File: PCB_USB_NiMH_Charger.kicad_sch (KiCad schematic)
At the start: 45 parts, among them J1 USB_C_Receptacle_Simple, J2 Conn_02x01, J3 Conn_02x01, J4 Conn_02x01, Q1 2SA1015, Q2 2SC1815, Q3 2SB834, Q4 2SC1815, Q5 2SB834, U1 LM393, U2 S-812C33A_TO92

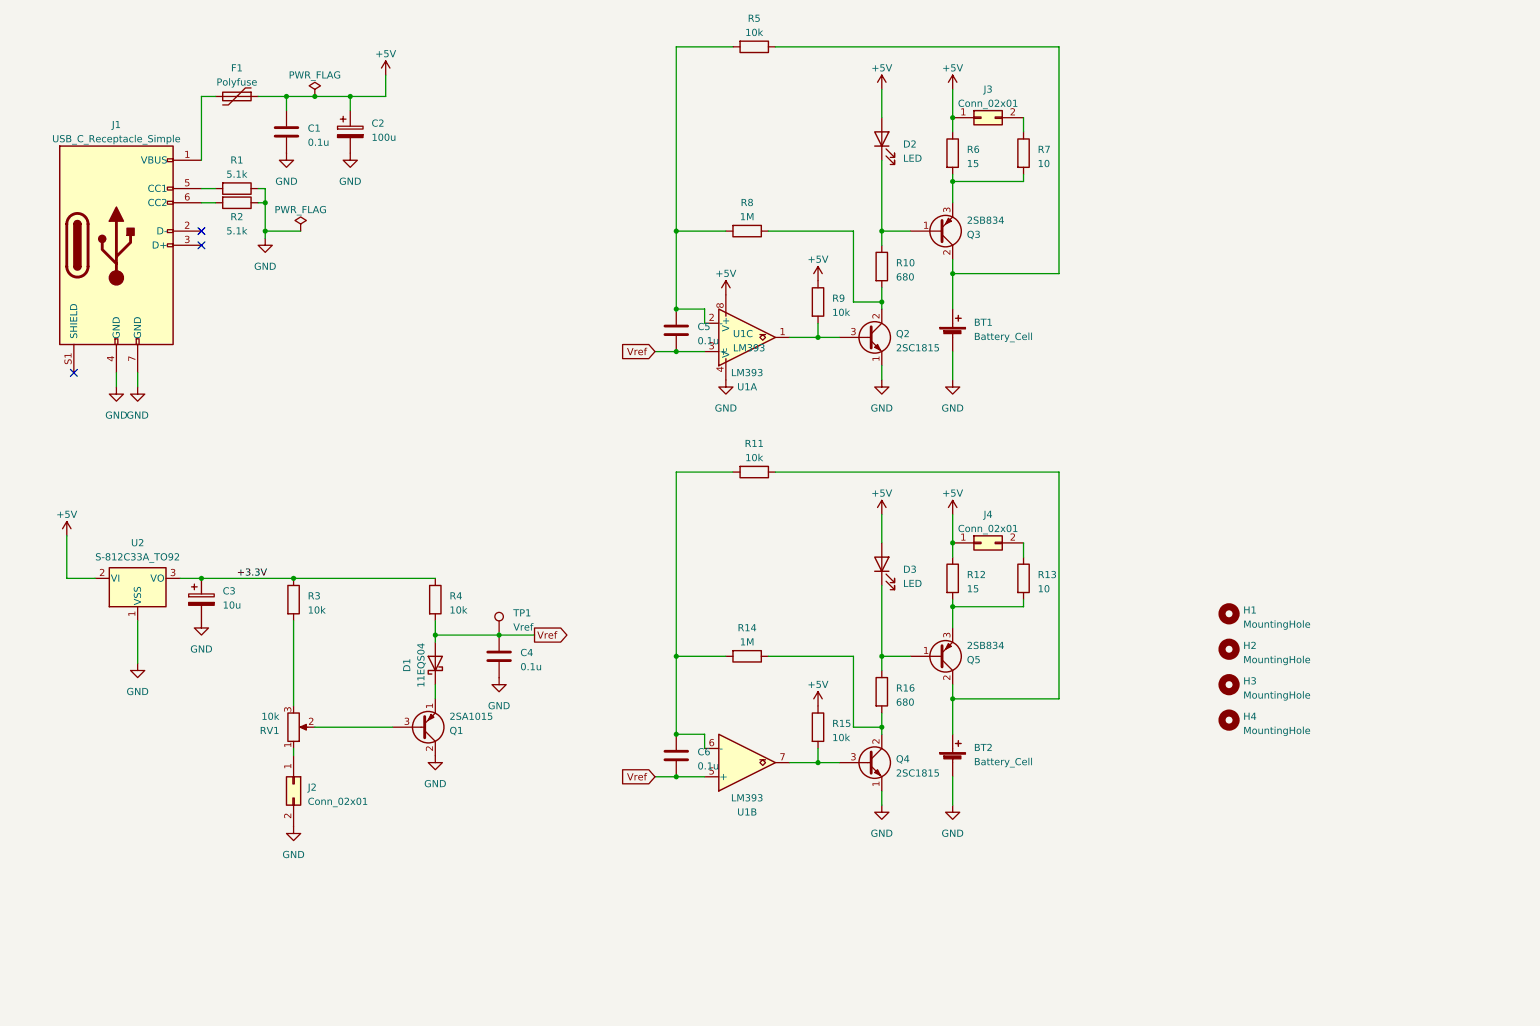
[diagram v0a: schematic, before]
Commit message: WIP: Change 2-battery circuit to 4-battery circuit
Change LM393 to LM339.
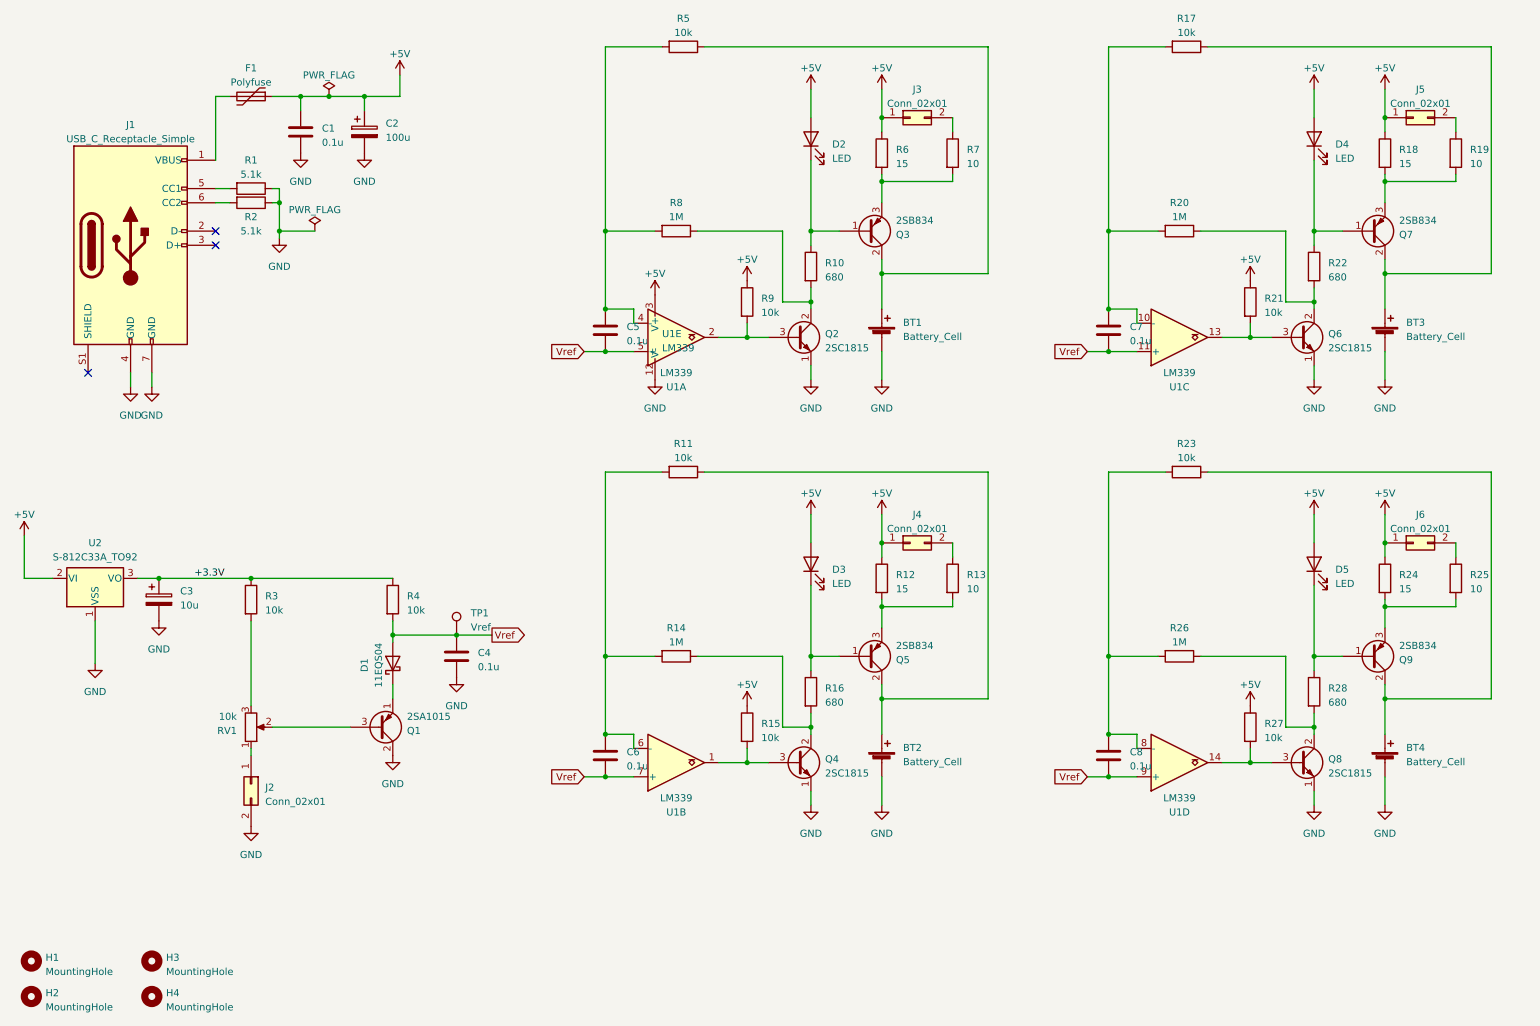
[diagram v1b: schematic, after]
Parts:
- removed U1: LM393, Package_DIP:DIP-8_W7.62mm_LongPads, symbol Comparator:LM393
- added BT3, BT4: Battery_Cell, Battery:BatteryHolder_Keystone_2460_1xAA, symbol Device:Battery_Cell
- added C7, C8: 0.1u, Capacitor_THT:C_Disc_D4.3mm_W1.9mm_P5.00mm, symbol Device:C
- added D4, D5: LED, LED_THT:LED_D5.0mm, symbol Device:LED
- added J5, J6: Conn_02x01, Connector_PinHeader_2.54mm:PinHeader_1x02_P2.54mm_Vertical, symbol Connector_Generic:Conn_02x01
- added Q6, Q8: 2SC1815, Package_TO_SOT_THT:TO-92_Inline_Wide, symbol Transistor_BJT:2SC1815
- added Q7, Q9: 2SB834, Package_TO_SOT_THT:TO-220-3_Vertical, symbol mylib:2SB834
- added R17, R21, R23, R27: 10k, Resistor_THT:R_Axial_DIN0207_L6.3mm_D2.5mm_P2.54mm_Vertical, symbol Device:R
- added R18, R24: 15, Resistor_THT:R_Axial_DIN0207_L6.3mm_D2.5mm_P2.54mm_Vertical, symbol Device:R
- added R19, R25: 10, Resistor_THT:R_Axial_DIN0207_L6.3mm_D2.5mm_P2.54mm_Vertical, symbol Device:R
- added R20, R26: 1M, Resistor_THT:R_Axial_DIN0207_L6.3mm_D2.5mm_P2.54mm_Vertical, symbol Device:R
- added R22, R28: 680, Resistor_THT:R_Axial_DIN0204_L3.6mm_D1.6mm_P5.08mm_Horizontal, symbol Device:R
- added U1: LM339, Package_DIP:DIP-14_W7.62mm_LongPads, symbol Comparator:LM339
- C2: footprint Capacitor_THT:CP_Radial_D6.3mm_P2.50mm -> Capacitor_THT:CP_Radial_D5.0mm_P2.50mm
- D1: footprint Diode_THT:D_DO-41_SOD81_P7.62mm_Horizontal -> Diode_THT:D_DO-41_SOD81_P2.54mm_Vertical_AnodeUp
- R1, R2: footprint Resistor_THT:R_Axial_DIN0204_L3.6mm_D1.6mm_P7.62mm_Horizontal -> Resistor_THT:R_Axial_DIN0204_L3.6mm_D1.6mm_P5.08mm_Horizontal
- R10, R16: footprint Resistor_THT:R_Axial_DIN0207_L6.3mm_D2.5mm_P7.62mm_Horizontal -> Resistor_THT:R_Axial_DIN0204_L3.6mm_D1.6mm_P5.08mm_Horizontal
- R11, R12, R13, R14, R15, R3, R4, R5, R6, R7, R8, R9: footprint Resistor_THT:R_Axial_DIN0207_L6.3mm_D2.5mm_P7.62mm_Horizontal -> Resistor_THT:R_Axial_DIN0207_L6.3mm_D2.5mm_P2.54mm_Vertical
- RV1: footprint mylib:Potentiometer_ACP_CA6-H2-3,5_Horizontal -> Potentiometer_THT:Potentiometer_ACP_CA6-H2,5_Horizontal
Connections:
- net +5V: now also D4.2 (A), D5.2 (A), J5.1 (Pin_1), J6.1 (Pin_1), R18.1, R21.1, R24.1, R27.1, U1.3 (V+)
- net GND: now also BT3.2 (-), BT4.2 (-), Q6.1 (E), Q8.1 (E), U1.12 (V-)
- net Vref: now also C7.2, C8.2, U1.11 (+), U1.5 (+), U1.7 (+), U1.9 (+)
- net at Q4.3 (B), R15.2: now also U1.1
- net at Q2.3 (B), R9.2: now also U1.2
- net at C6.1, R11.2, R14.2: now also U1.6 (-)
- net at C5.1, R5.2, R8.2: now also U1.4 (-)
- new net: D5.1 (K), Q9.1 (B), R28.1
- new net: Q8.2 (C), R26.1, R28.2
- new net: J5.2 (Pin_2), R19.1
- new net: Q7.3 (E), R18.2, R19.2
- new net: Q8.3 (B), R27.2, U1.14
- new net: C8.1, R23.2, R26.2, U1.8 (-)
- new net: BT4.1 (+), Q9.2 (C), R23.1
- new net: Q9.3 (E), R24.2, R25.2
- new net: J6.2 (Pin_2), R25.1
- new net: Q6.2 (C), R20.1, R22.2
- new net: Q6.3 (B), R21.2, U1.13
- new net: C7.1, R17.2, R20.2, U1.10 (-)
- new net: D4.1 (K), Q7.1 (B), R22.1
- new net: BT3.1 (+), Q7.2 (C), R17.1
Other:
- title: USB NiMH slow charger -> USB NiMH slow charger (for 4 battery cells)
- moved on the sheet: BT1, BT2, C1, C2, C3, C4, C5, C6, D1, D2, D3, F1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

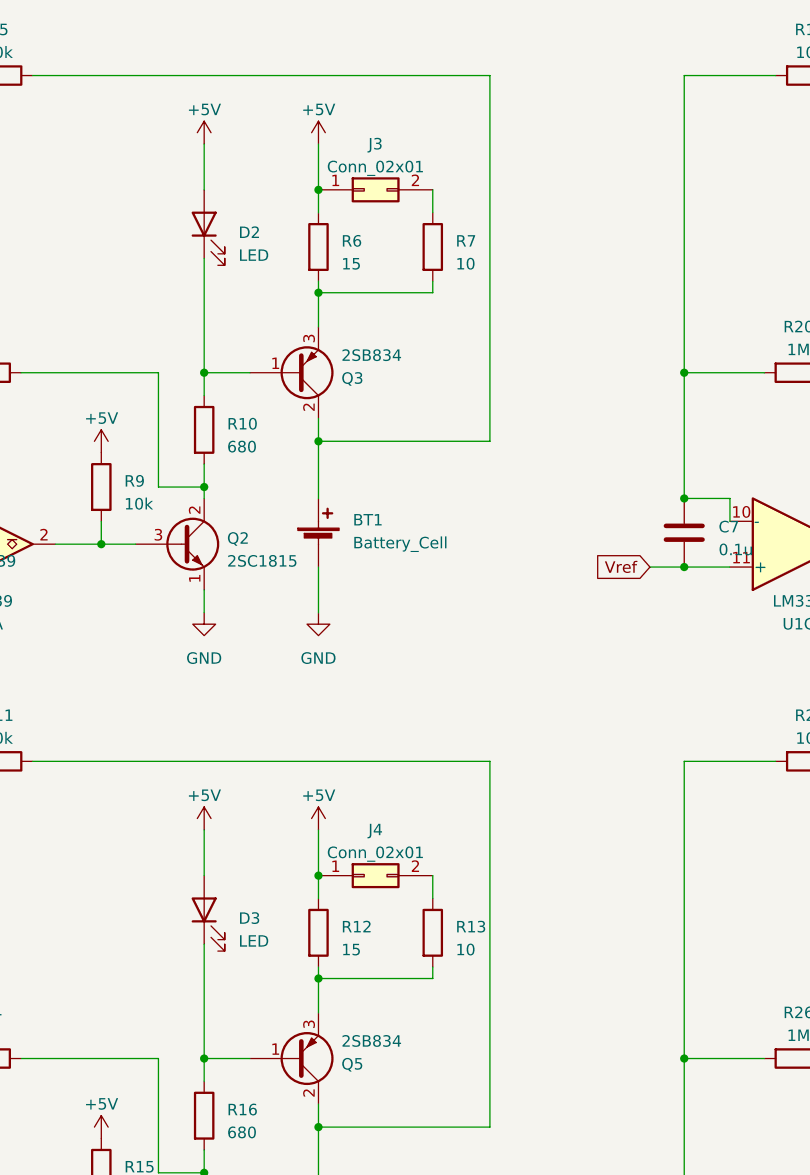
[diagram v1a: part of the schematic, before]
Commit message: Change BT1 and BT2 to AAA from AA
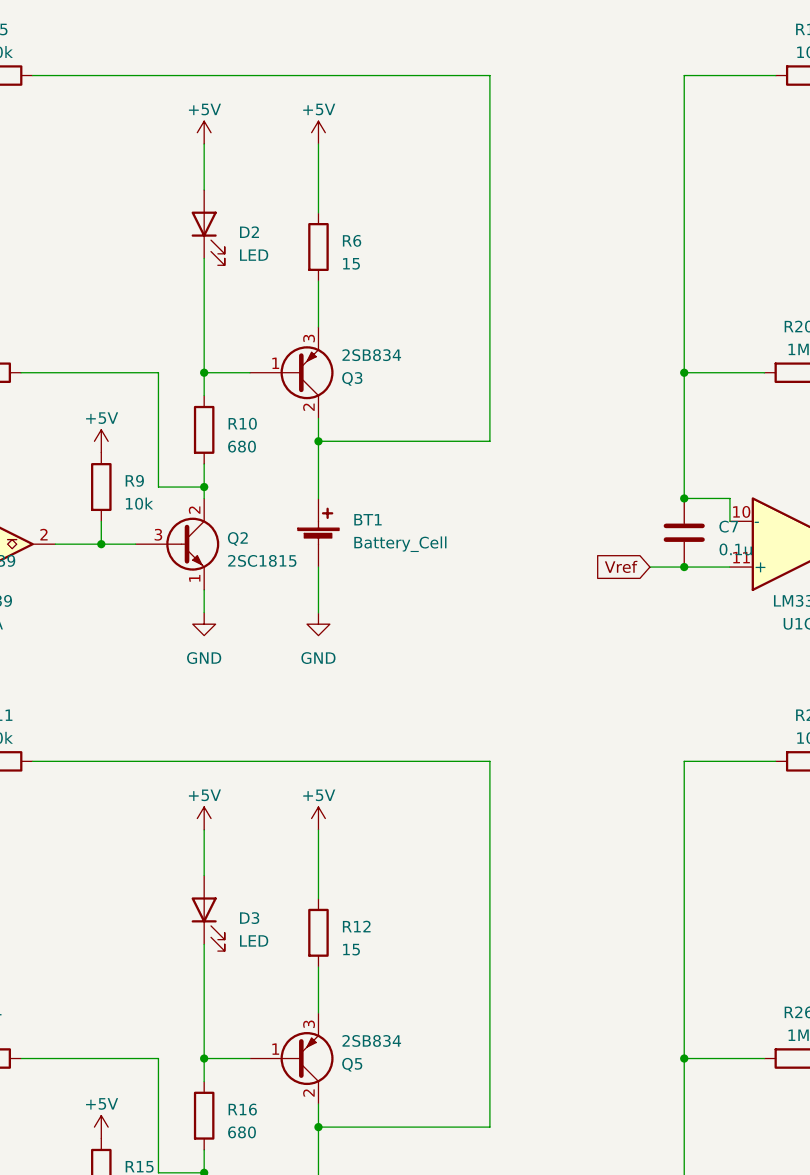
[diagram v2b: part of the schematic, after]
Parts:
- removed J3, J4: Conn_02x01, Connector_PinHeader_2.54mm:PinHeader_1x02_P2.54mm_Vertical, symbol Connector_Generic:Conn_02x01
- removed R13, R7: 10, Resistor_THT:R_Axial_DIN0207_L6.3mm_D2.5mm_P2.54mm_Vertical, symbol Device:R
- BT1, BT2: footprint Battery:BatteryHolder_Keystone_2460_1xAA -> Battery:BatteryHolder_Keystone_2466_1xAAA
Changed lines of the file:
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@@
   (junction (at 77.47 30.48) (diameter 0) (color 0 0 0 0)
   )
-  (junction (at 170.18 110.49) (diameter 0) (color 0 0 0 0)
-  )
   (junction (at 71.12 30.48) (diameter 0) (color 0 0 0 0)
   )
@@
   (junction (at 210.82 68.58) (diameter 0) (color 0 0 0 0)
   )
-  (junction (at 170.18 34.29) (diameter 0) (color 0 0 0 0)
-  )
   (junction (at 57.15 116.84) (diameter 0) (color 0 0 0 0)
   )
@@
   (junction (at 210.82 152.4) (diameter 0) (color 0 0 0 0)
   )
-  (junction (at 170.18 45.72) (diameter 0) (color 0 0 0 0)
-  )
   (junction (at 146.05 73.66) (diameter 0) (color 0 0 0 0)
   )
@@
   (junction (at 120.65 54.61) (diameter 0) (color 0 0 0 0)
   )
-  (junction (at 170.18 121.92) (diameter 0) (color 0 0 0 0)
-  )
   (junction (at 247.65 130.81) (diameter 0) (color 0 0 0 0)
   )
@@
     (stroke (width 0) (type default))
   )
-  (wire (pts (xy 170.18 34.29) (xy 170.18 36.83))
+  (wire (pts (xy 170.18 29.21) (xy 170.18 36.83))
     (stroke (width 0) (type default))
   )
@@
     (stroke (width 0) (type default))
   )
-  (wire (pts (xy 170.18 105.41) (xy 170.18 110.49))
+  (wire (pts (xy 170.18 105.41) (xy 170.18 113.03))
     (stroke (width 0) (type default))
   )
@@
     (stroke (width 0) (type default))
   )
-  (wire (pts (xy 182.88 113.03) (xy 182.88 110.49))
-    (stroke (width 0) (type default))
-  )
   (wire (pts (xy 189.23 21.59) (xy 189.23 62.23))
     (stroke (width 0) (type default))
@@
     (stroke (width 0) (type default))
   )
-  (wire (pts (xy 170.18 110.49) (xy 170.18 113.03))
-    (stroke (width 0) (type default))
-  )
   (wire (pts (xy 157.48 130.81) (xy 157.48 133.35))
     (stroke (width 0) (type default))
@@
     (stroke (width 0) (type default))
   )
-  (wire (pts (xy 182.88 120.65) (xy 182.88 121.92))
-    (stroke (width 0) (type default))
-  )
   (wire (pts (xy 152.4 130.81) (xy 152.4 143.51))
     (stroke (width 0) (type default))
   )
-  (wire (pts (xy 170.18 29.21) (xy 170.18 34.29))
-    (stroke (width 0) (type default))
-  )
   (wire (pts (xy 247.65 105.41) (xy 247.65 110.49))
     (stroke (width 0) (type default))
@@
     (stroke (width 0) (type default))
   )
-  (wire (pts (xy 182.88 121.92) (xy 170.18 121.92))
-    (stroke (width 0) (type default))
-  )
   (wire (pts (xy 116.84 76.2) (xy 120.65 76.2))
     (stroke (width 0) (type default))
@@
     (stroke (width 0) (type default))
   )
-  (wire (pts (xy 182.88 44.45) (xy 182.88 45.72))
-    (stroke (width 0) (type default))
-  )
   (wire (pts (xy 130.81 21.59) (xy 120.65 21.59))
     (stroke (width 0) (type default))
@@
     (stroke (width 0) (type default))
   )
-  (wire (pts (xy 182.88 36.83) (xy 182.88 34.29))
-    (stroke (width 0) (type default))
-  )
   (wire (pts (xy 207.01 152.4) (xy 210.82 152.4))
     (stroke (width 0) (type default))
@@
     (stroke (width 0) (type default))
   )
-  (wire (pts (xy 170.18 45.72) (xy 170.18 49.53))
+  (wire (pts (xy 170.18 44.45) (xy 170.18 49.53))
     (stroke (width 0) (type default))
   )
@@
     (stroke (width 0) (type default))
   )
-  (wire (pts (xy 182.88 45.72) (xy 170.18 45.72))
-    (stroke (width 0) (type default))
-  )
   (wire (pts (xy 247.65 157.48) (xy 247.65 154.94))
     (stroke (width 0) (type default))
@@
     (stroke (width 0) (type default))
   )
-  (wire (pts (xy 170.18 121.92) (xy 170.18 125.73))
-    (stroke (width 0) (type default))
-  )
   (wire (pts (xy 146.05 147.32) (xy 146.05 149.86))
     (stroke (width 0) (type default))
@@
     (stroke (width 0) (type default))
   )
-  (wire (pts (xy 170.18 44.45) (xy 170.18 45.72))
-    (stroke (width 0) (type default))
-  )
   (wire (pts (xy 247.65 54.61) (xy 252.73 54.61))
     (stroke (width 0) (type default))
@@
     (stroke (width 0) (type default))
   )
-  (wire (pts (xy 170.18 120.65) (xy 170.18 121.92))
+  (wire (pts (xy 170.18 120.65) (xy 170.18 125.73))
     (stroke (width 0) (type default))
   )
@@
     )
   )
-  (symbol (lib_id "Connector_Generic:Conn_02x01") (at 175.26 110.49 0) (unit 1)
-    (in_bom yes) (on_board yes) (dnp no) (fields_autoplaced)
-    (property "Reference" "J4" (at 176.53 105.41 0)
-      (effects (font (size 1.27 1.27)))
-    )
-    (property "Value" "Conn_02x01" (at 176.53 107.95 0)
-      (effects (font (size 1.27 1.27)))
-    )
-    (property "Footprint" "Connector_PinHeader_2.54mm:PinHeader_1x02_P2.54mm_Vertical" (at 175.26 110.49 0)
-      (effects (font (size 1.27 1.27)) hide)
-    )
-    (property "Datasheet" "~" (at 175.26 110.49 0)
-      (effects (font (size 1.27 1.27)) hide)
-    )
-    (pin "1")
-    (pin "2")
-    (instances
-      (project "PCB_USB_NiMH_Charger"
-        (path "/8896e7f7-a0e4-43c2-91c1-4a5c563995a5"
-          (reference "J4") (unit 1)
-        )
-      )
-    )
-  )
   (symbol (lib_id "power:GND") (at 35.56 82.55 0) (unit 1)
     (in_bom yes) (on_board yes) (dnp no) (fields_autoplaced)
@@
       (effects (font (size 1.27 1.27)) (justify left))
     )
-    (property "Footprint" "Battery:BatteryHolder_Keystone_2460_1xAA" (at 170.18 72.136 90)
+    (property "Footprint" "Battery:BatteryHolder_Keystone_2466_1xAAA" (at 170.18 72.136 90)
       (effects (font (size 1.27 1.27)) hide)
     )
@@
     )
   )
-  (symbol (lib_id "Device:R") (at 182.88 116.84 0) (unit 1)
-    (in_bom yes) (on_board yes) (dnp no) (fields_autoplaced)
-    (property "Reference" "R13" (at 185.42 116.205 0)
-      (effects (font (size 1.27 1.27)) (justify left))
-    )
-    (property "Value" "10" (at 185.42 118.745 0)
-      (effects (font (size 1.27 1.27)) (justify left))
-    )
-    (property "Footprint" "Resistor_THT:R_Axial_DIN0207_L6.3mm_D2.5mm_P2.54mm_Vertical" (at 181.102 116.84 90)
-      (effects (font (size 1.27 1.27)) hide)
-    )
-    (property "Datasheet" "~" (at 182.88 116.84 0)
-      (effects (font (size 1.27 1.27)) hide)
-    )
-    (pin "1")
-    (pin "2")
-    (instances
-      (project "PCB_USB_NiMH_Charger"
-        (path "/8896e7f7-a0e4-43c2-91c1-4a5c563995a5"
-          (reference "R13") (unit 1)
-        )
-      )
-    )
-  )
   (symbol (lib_id "Transistor_BJT:2SC1815") (at 245.11 73.66 0) (unit 1)
     (in_bom yes) (on_board yes) (dnp no) (fields_autoplaced)
@@
     )
   )
-  (symbol (lib_id "Connector_Generic:Conn_02x01") (at 175.26 34.29 0) (unit 1)
-    (in_bom yes) (on_board yes) (dnp no) (fields_autoplaced)
-    (property "Reference" "J3" (at 176.53 29.21 0)
-      (effects (font (size 1.27 1.27)))
-    )
-    (property "Value" "Conn_02x01" (at 176.53 31.75 0)
-      (effects (font (size 1.27 1.27)))
-    )
-    (property "Footprint" "Connector_PinHeader_2.54mm:PinHeader_1x02_P2.54mm_Vertical" (at 175.26 34.29 0)
-      (effects (font (size 1.27 1.27)) hide)
-    )
-    (property "Datasheet" "~" (at 175.26 34.29 0)
-      (effects (font (size 1.27 1.27)) hide)
-    )
-    (pin "1")
-    (pin "2")
-    (instances
-      (project "PCB_USB_NiMH_Charger"
-        (path "/8896e7f7-a0e4-43c2-91c1-4a5c563995a5"
-          (reference "J3") (unit 1)
-        )
-      )
-    )
-  )
-  (symbol (lib_id "Device:R") (at 182.88 40.64 0) (unit 1)
-    (in_bom yes) (on_board yes) (dnp no) (fields_autoplaced)
-    (property "Reference" "R7" (at 185.42 40.005 0)
-      (effects (font (size 1.27 1.27)) (justify left))
-    )
-    (property "Value" "10" (at 185.42 42.545 0)
-      (effects (font (size 1.27 1.27)) (justify left))
-    )
-    (property "Footprint" "Resistor_THT:R_Axial_DIN0207_L6.3mm_D2.5mm_P2.54mm_Vertical" (at 181.102 40.64 90)
-      (effects (font (size 1.27 1.27)) hide)
-    )
-    (property "Datasheet" "~" (at 182.88 40.64 0)
-      (effects (font (size 1.27 1.27)) hide)
-    )
-    (pin "1")
-    (pin "2")
-    (instances
-      (project "PCB_USB_NiMH_Charger"
-        (path "/8896e7f7-a0e4-43c2-91c1-4a5c563995a5"
-          (reference "R7") (unit 1)
-        )
-      )
-    )
-  )
   (symbol (lib_id "power:GND") (at 39.37 82.55 0) (unit 1)
     (in_bom yes) (on_board yes) (dnp no) (fields_autoplaced)
@@
       (effects (font (size 1.27 1.27)) (justify left))
     )
-    (property "Footprint" "Battery:BatteryHolder_Keystone_2460_1xAA" (at 170.18 148.336 90)
+    (property "Footprint" "Battery:BatteryHolder_Keystone_2466_1xAAA" (at 170.18 148.336 90)
       (effects (font (size 1.27 1.27)) hide)
     )
